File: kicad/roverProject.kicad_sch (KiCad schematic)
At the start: 8 parts, among them M1 DC Motor w/ Encoder, M2 DC Motor w/ Encoder, U1 MPU-6050

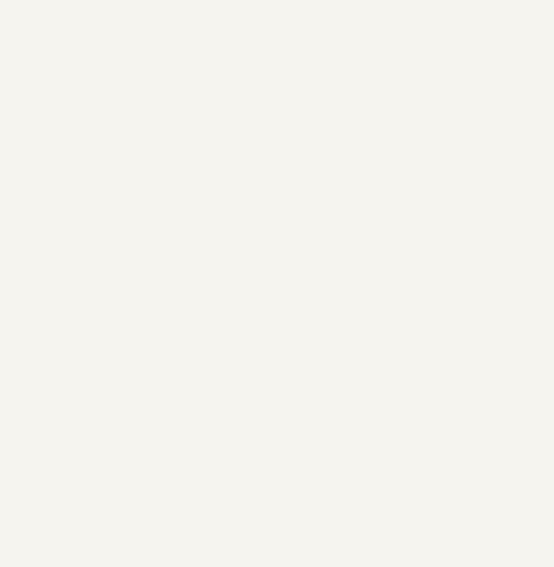
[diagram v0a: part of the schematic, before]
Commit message: Create pid-controller.cpp and Update manual-control.py
Amend motor-control.h to externalize motor values
Create pid-controller.h
Create pid-controller.cpp
Amend main.cpp to organise into function calls
Amend motor-control.cpp to remove redundant checks
Update serial-control.cpp to add feedback communication
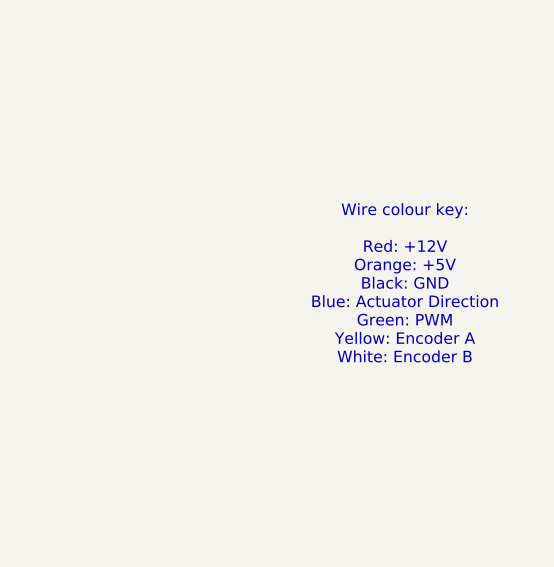
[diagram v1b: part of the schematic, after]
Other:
- note added: "Wire colour key: Red: +12V Orange: +5V Black: GND Blue: Actuator Direction Green: PWM Yellow: Encoder A White: Encoder B"
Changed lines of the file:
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@@
 		(rev "V0.1")
+	)
+	(text "Wire colour key:\n\nRed: +12V\nOrange: +5V\nBlack: GND\nBlue: Actuator Direction\nGreen: PWM\nYellow: Encoder A\nWhite: Encoder B\n\n"
+		(exclude_from_sim no)
+		(at 263.652 148.336 0)
+		(effects
+			(font
+				(size 1.27 1.27)
+			)
+		)
 	)
 	(junction
@@
 			(width 0)
 			(type default)
+			(color 255 255 0 1)
 		)
 	)
@@
 			(width 0)
 			(type default)
+			(color 0 0 0 1)
 		)
 	)
@@
 			(width 0)
 			(type default)
+			(color 255 255 0 1)
 		)
 	)
@@
 			(width 0)
 			(type default)
-			(color 255 0 0 1)
+			(color 255 153 0 1)
 		)
 	)
@@
 			(width 0)
 			(type default)
+			(color 255 255 0 1)
 		)
 	)
@@
 			(width 0)
 			(type default)
+			(color 0 0 0 1)
 		)
 	)
@@
 			(width 0)
 			(type default)
+			(color 255 255 255 1)
 		)
 	)
@@
 			(width 0)
 			(type default)
+			(color 0 0 255 1)
 		)
 	)
@@
 			(width 0)
 			(type default)
+			(color 255 0 0 1)
 		)
 	)
@@
 			(width 0)
 			(type default)
+			(color 255 255 255 1)
 		)
 	)
@@
 			(width 0)
 			(type default)
+			(color 0 0 255 1)
 		)
 	)
@@
 			(width 0)
 			(type default)
+			(color 255 255 255 1)
 		)
 	)
@@
 			(width 0)
 			(type default)
+			(color 255 0 0 1)
 		)
 	)
@@
 			(width 0)
 			(type default)
+			(color 0 0 0 1)
 		)
 	)
@@
 			(width 0)
 			(type default)
+			(color 0 194 0 1)
 		)
 	)
@@
 			(width 0)
 			(type default)
+			(color 0 0 0 1)
 		)
 	)
@@
 			(width 0)
 			(type default)
+			(color 255 255 255 1)
 		)
 	)
@@
 			(width 0)
 			(type default)
+			(color 0 194 0 1)
 		)
 	)
@@
 			(width 0)
 			(type default)
+			(color 255 0 0 1)
 		)
 	)
@@
 			(width 0)
 			(type default)
-			(color 255 0 0 1)
+			(color 255 153 0 1)
 		)
 	)
@@
 			(width 0)
 			(type default)
+			(color 255 0 0 1)
 		)
 	)
@@
 			(width 0)
 			(type default)
-			(color 255 0 0 1)
+			(color 255 153 0 1)
 		)
 	)
@@
 			(width 0)
 			(type default)
-		)
-	)
+			(color 255 255 0 1)
+		)
+	)
